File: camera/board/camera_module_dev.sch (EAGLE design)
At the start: 11 parts, among them IC1 74541PW, IC2 74541PW, Q1 MOSFET-NCHANNELBSS123LT1G, Q2 MOSFET-NCHANNELBSS123LT1G

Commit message: Schematic more or less done, moving to layout
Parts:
- added C1: 2.2uF, biomimetic:CAP0402-CAP
- added C10, C11, C12, C7: 1uF, biomimetic:CAP0603-CAP
- added C13, C14, C15, C16, C5, C6, C8, C9: 100nF, biomimetic:CAP0402-CAP
- added C2, C3: 1uF, biomimetic:CAP0402-CAP
- added C4: 10nF, biomimetic:CAP0402-CAP
- added JP3, JP4: (no value), pinhead:PINHD-1X9
- added L1, L2: 3.3uH, biomimetic:INDUCTOR1007
- added R1: 18k, biomimetic:RESISTOR0402-RES
- added R10, R11, R8, R9: 4k7, biomimetic:RESISTOR0402-RES
- added R2: 18k/5k, biomimetic:RESISTOR0402-RES
- added R3, R4, R7: 10k, biomimetic:RESISTOR0402-RES
- added R5: (no value), biomimetic:RESISTOR0402-RES
- added R6: 1k8, biomimetic:RESISTOR0402-RES
- added SJ1, SJ10, SJ11, SJ2, SJ3, SJ4, SJ5, SJ6, SJ7, SJ8, SJ9: SOLDERJUMPERNO, SparkFun-Passives:SOLDERJUMPERNO
- added SJ12, SJ13, SJ14: (no value), SparkFun-Passives:SOLDERJUMPER_2WAYS
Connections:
- new net +3V3: C1.1, C5.2, C6.2, IC1P.VCC, IC2P.VCC, R11.1, R5.1, R9.1, SJ12.3, SJ13.3, U$3G$2.AVDD, U$4.6, U$6G$1.V+
- new net D0: IC1A.A1, SJ1.2, U$1G$1.DATA0, U$2G$1.DATA0, U$3G$1.DATA0
- new net D1: IC1A.A2, SJ2.2, U$1G$1.DATA1, U$2G$1.DATA1, U$3G$1.DATA1
- new net D2: IC1A.A3, SJ3.2, U$1G$1.DATA2, U$2G$1.DATA2, U$3G$1.DATA2
- new net D3: IC1A.A4, SJ4.2, U$1G$1.DATA3, U$2G$1.DATA3, U$3G$1.DATA3
- new net D4: IC1A.A5, SJ5.2, U$1G$1.DATA4, U$2G$1.DATA4, U$3G$1.DATA4
- new net D5: IC1A.A6, SJ6.2, U$1G$1.DATA5, U$2G$1.DATA5, U$3G$1.DATA5
- new net D6: IC1A.A7, SJ7.2, U$1G$1.DATA6, U$2G$1.DATA6, U$3G$1.DATA6
- new net D7: IC1A.A8, SJ8.2, U$1G$1.DATA7, U$2G$1.DATA7, U$3G$1.DATA7
- new net GND: C1.2, C10.2, C11.1, C12.2, C13.2, C14.1, C15.1, C16.2, C2.2, C3.2, C4.1, C5.1, C6.1, C7.1, C8.2, C9.2, IC1P.GND, IC2A.A4, IC2A.A5, IC2A.A6, IC2A.A7, IC2A.A8, IC2P.GND, JP3.9, JP4.9, QG1.VSS, R3.2, R4.2, R7.1, SJ12.1, SJ13.1, U$1G$2.GND, U$2G$2.GND, U$2IOVSS.V, U$3G$2.GND, U$4.11, U$5.11, U$6G$1.GND
- new net HSYNC: IC2A.A3, SJ11.2, U$1G$1.HREF, U$2G$1.HREF, U$3G$1.HREF
- new net N$1: QG1.OUT, SJ14.3
- new net N$10: IC2A.G1, SJ12.2
- new net N$19: R1.2, R4.1, U$6LDOB.FB
- new net N$2: JP3.8, U$4.10
- new net N$21: R2.2, R3.1, U$6LDOA.FB
- new net N$3: R6.1, R7.2, SJ14.1
- new net N$4: C13.1, U$1VREF2.V
- new net N$5: C9.1, U$1VREF1.V
- new net N$6: C12.1, C14.2, C16.1, C7.2, L2.2, U$1G$2.AVDD, U$2G$2.DVDD
- new net N$7: IC1A.G1, SJ13.2
- new net N$8: C10.1, C11.2, C15.2, C8.1, L1.2, U$1G$2.DVDD, U$2G$2.AVDD, U$2IOVDD.V
- new net PCLK: IC2A.A1, SJ9.2, U$1G$1.PCLK, U$2G$1.PCLK, U$3G$1.PCLK
- new net PMOD_D0: IC1A.Y1, JP4.1, SJ1.1, U$5.1
- new net PMOD_D1: IC1A.Y2, JP4.2, SJ2.1, U$5.2
- new net PMOD_D2: IC1A.Y3, JP4.3, SJ3.1, U$5.3
- new net PMOD_D3: IC1A.Y4, JP4.4, SJ4.1, U$5.4
- new net PMOD_D4: IC1A.Y5, JP4.5, SJ5.1, U$5.7
- new net PMOD_D5: IC1A.Y6, JP4.6, SJ6.1, U$5.8
- new net PMOD_D6: IC1A.Y7, IC1A.Y8, JP4.7, SJ7.1, SJ8.1, U$5.9
- new net PMOD_D7: JP4.8, U$5.10
- new net PMOD_HSYNC: IC2A.Y3, JP3.7, SJ11.1, U$4.9
- new net PMOD_PCLK: IC2A.Y1, JP3.5, SJ9.1, U$4.7
- new net PMOD_RESET: IC1A.G2, IC2A.G2, JP3.1, QG1.CON, R5.2, U$1G$1.PWDN, U$2G$1.PWDN, U$3G$1.PWDN, U$4.1, U$6CTRL.EN
- new net PMOD_SCL: JP3.3, Q2.D, R9.2, U$4.3
- new net PMOD_SDA: JP3.4, Q1.D, R11.2, U$4.4
- new net PMOD_VSYNC: IC2A.Y2, JP3.6, SJ10.1, U$4.8
- new net PMOD_XCLK: JP3.2, R6.2, U$4.2
- new net SCL: Q2.S, R8.2, U$1G$1.SCL, U$2G$1.SCL, U$3G$1.SCL
- new net SDA: Q1.S, R10.2, U$1G$1.SDA, U$2G$1.SDA, U$3G$1.SDA
- new net VCCIO: C2.1, C4.2, L1.1, Q1.G, Q2.G, QG1.VDD, R1.1, R10.1, R8.1, U$6LDOB.OUT
- new net VDD: C3.1, L2.1, R2.1, U$6LDOA.OUT
- new net VSYNC: IC2A.A2, SJ10.2, U$1G$1.VSYNC, U$2G$1.VSYNC, U$3G$1.VSYNC
- new net XCLK: SJ14.2, U$1G$1.XVCLK, U$2G$1.XVCLK, U$3G$1.XVCLK
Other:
- moved on the sheet: IC1, IC2, Q1, Q2, QG1, U$1VREF1, U$1VREF2, U$2IOVDD, U$2IOVSS, U$4, U$6CTRL, U$6LDOA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

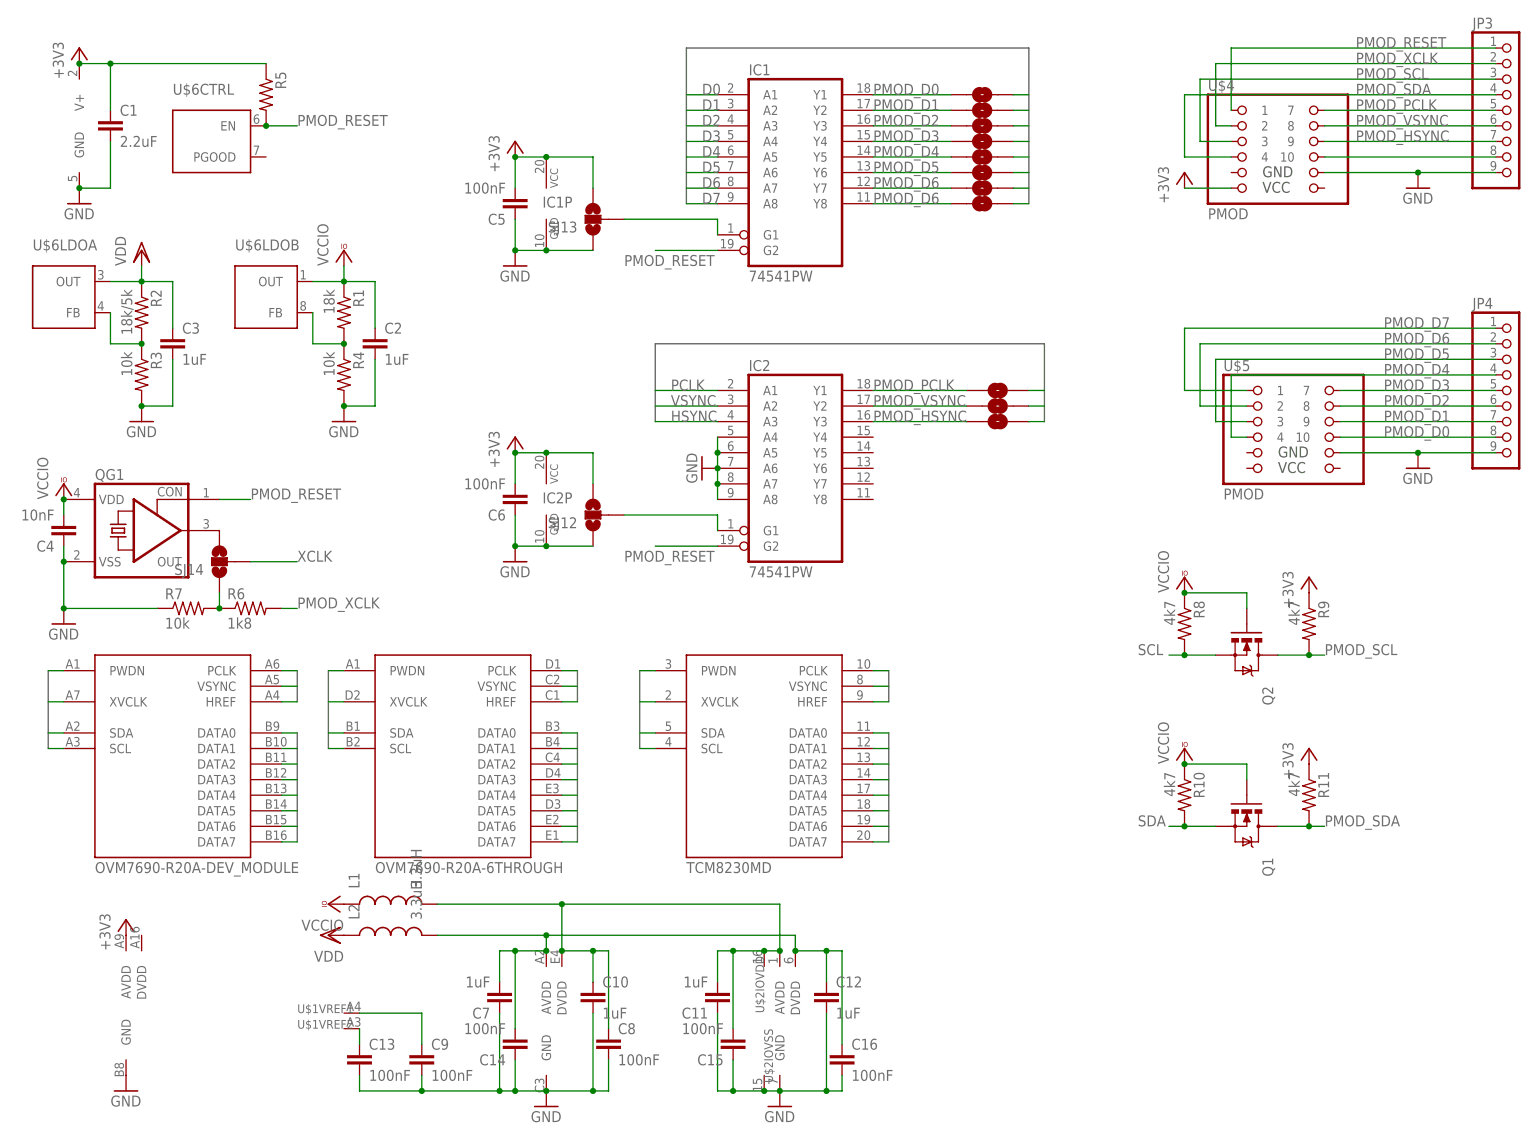
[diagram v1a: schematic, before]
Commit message: Pmod signal routing more or less done
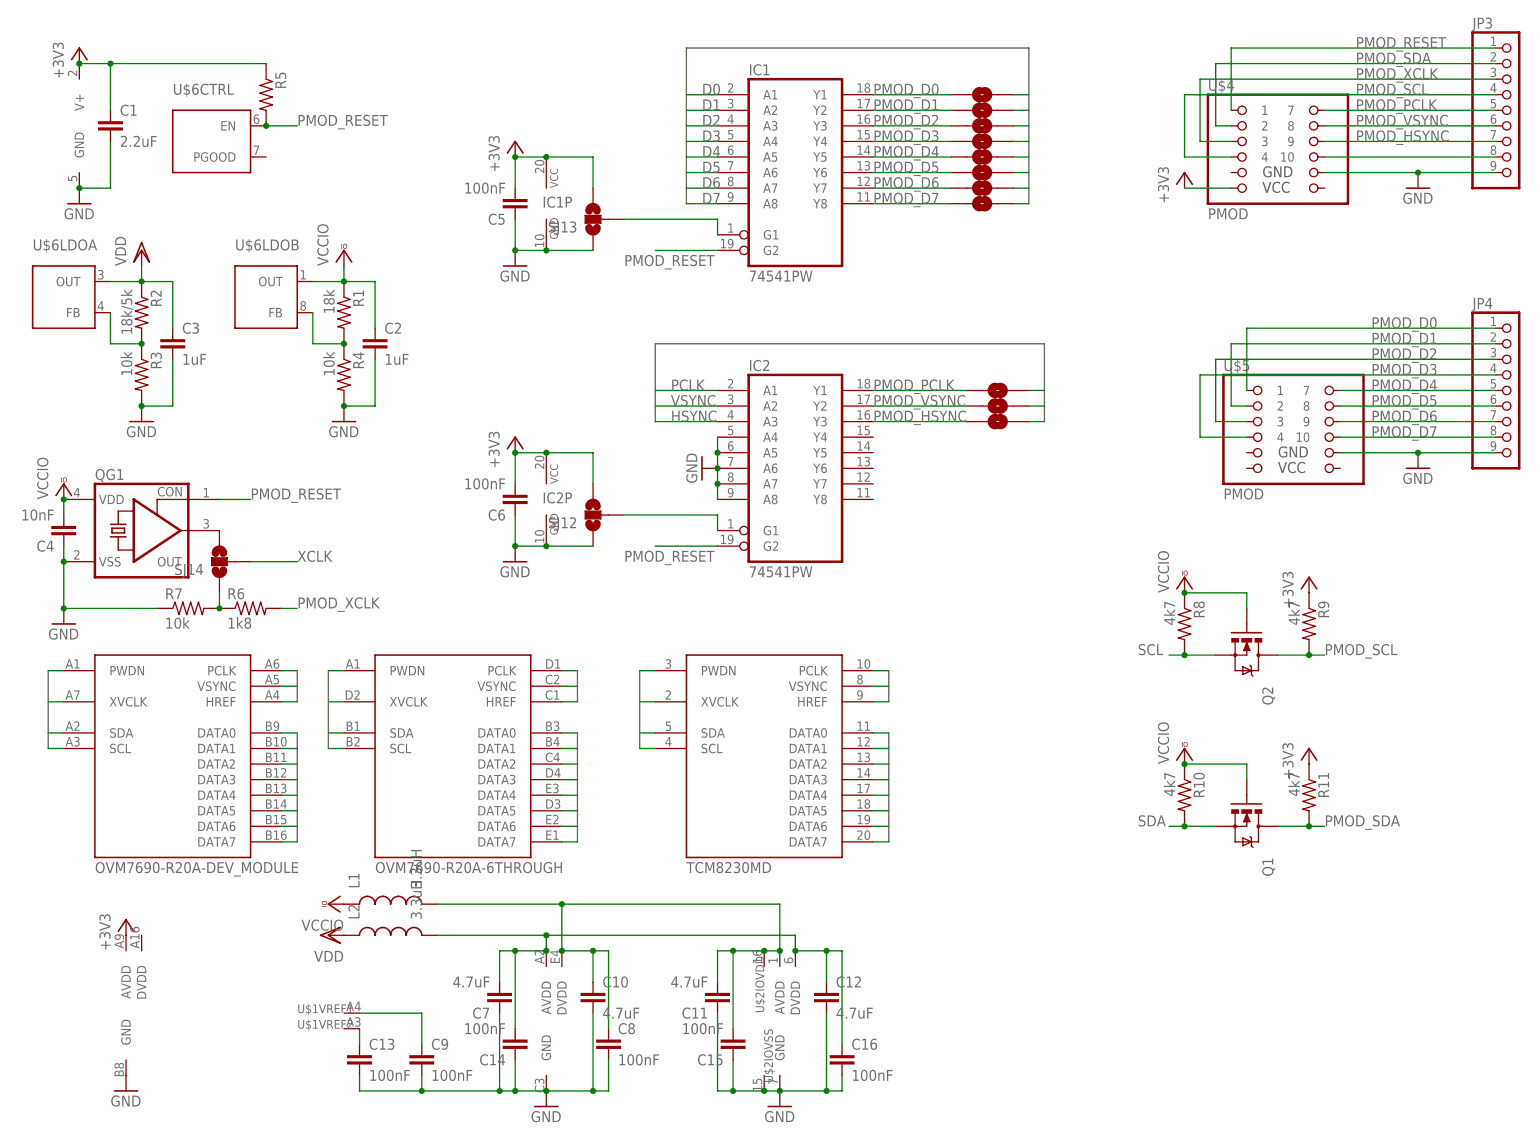
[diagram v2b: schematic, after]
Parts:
- C10, C11, C12, C7: value 1uF -> 4.7uF
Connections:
- net PMOD_D6: no longer IC1A.Y8, SJ8.1
- net PMOD_D7: now also IC1A.Y8, SJ8.1
- net PMOD_SCL: now also JP3.4, U$4.4; no longer JP3.3, U$4.3
- net PMOD_SDA: now also JP3.2, U$4.2; no longer JP3.4, U$4.4
- net PMOD_XCLK: now also JP3.3, U$4.3; no longer JP3.2, U$4.2

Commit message: Most layout done
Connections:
- net +3V3: now also U$3G$2.DVDD; no longer U$3G$2.AVDD
- net N$19: now also U$6LDOA.FB; no longer U$6LDOB.FB
- net N$21: now also U$6LDOB.FB; no longer U$6LDOA.FB
- net VCCIO: now also U$6LDOA.OUT; no longer U$6LDOB.OUT
- net VDD: now also U$6LDOB.OUT; no longer U$6LDOA.OUT
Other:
- moved on the sheet: U$6LDOA, U$6LDOB
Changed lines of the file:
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@@
 <instance part="U$6" gate="G$1" x="10.16" y="165.1"/>
 <instance part="U$6" gate="CTRL" x="38.1" y="157.48"/>
-<instance part="U$6" gate="LDOB" x="45.72" y="132.08"/>
-<instance part="U$6" gate="LDOA" x="12.7" y="132.08"/>
+<instance part="U$6" gate="LDOA" x="45.72" y="132.08"/>
+<instance part="U$6" gate="LDOB" x="12.7" y="132.08"/>
 <instance part="Q1" gate="G$1" x="200.66" y="50.8" smashed="yes" rot="R270">
 <attribute name="NAME" x="203.2" y="45.72" size="1.778" layer="95" rot="R270"/>
@@
 <instance part="VCC4" gate="G$1" x="190.5" y="63.5"/>
 <instance part="GND9" gate="1" x="111.76" y="109.22" rot="R270"/>
-<instance part="+3V7" gate="G$1" x="17.78" y="35.56"/>
+<instance part="+3V7" gate="G$1" x="20.32" y="38.1"/>
 <instance part="GND10" gate="1" x="17.78" y="7.62"/>
 <instance part="GND11" gate="1" x="86.36" y="5.08"/>
@@
 </segment>
 <segment>
-<pinref part="U$3" gate="G$2" pin="AVDD"/>
+<pinref part="U$3" gate="G$2" pin="DVDD"/>
 <pinref part="+3V7" gate="G$1" pin="+3V3"/>
+<wire x1="20.32" y1="33.02" x2="20.32" y2="35.56" width="0.1524" layer="91"/>
 </segment>
 </net>
@@
 <pinref part="R1" gate="G$1" pin="2"/>
 <pinref part="R4" gate="G$1" pin="1"/>
-<pinref part="U$6" gate="LDOB" pin="FB"/>
+<pinref part="U$6" gate="LDOA" pin="FB"/>
 <wire x1="48.26" y1="134.62" x2="48.26" y2="129.54" width="0.1524" layer="91"/>
 <wire x1="48.26" y1="129.54" x2="53.34" y2="129.54" width="0.1524" layer="91"/>
@@
 <pinref part="R2" gate="G$1" pin="2"/>
 <pinref part="R3" gate="G$1" pin="1"/>
-<pinref part="U$6" gate="LDOA" pin="FB"/>
+<pinref part="U$6" gate="LDOB" pin="FB"/>
 <wire x1="20.32" y1="129.54" x2="15.24" y2="129.54" width="0.1524" layer="91"/>
 <wire x1="15.24" y1="129.54" x2="15.24" y2="134.62" width="0.1524" layer="91"/>
@@
 <net name="VDD" class="0">
 <segment>
-<pinref part="U$6" gate="LDOA" pin="OUT"/>
+<pinref part="U$6" gate="LDOB" pin="OUT"/>
 <pinref part="R2" gate="G$1" pin="1"/>
 <wire x1="15.24" y1="139.7" x2="20.32" y2="139.7" width="0.1524" layer="91"/>
@@
 <net name="VCCIO" class="0">
 <segment>
-<pinref part="U$6" gate="LDOB" pin="OUT"/>
+<pinref part="U$6" gate="LDOA" pin="OUT"/>
 <pinref part="R1" gate="G$1" pin="1"/>
 <wire x1="48.26" y1="139.7" x2="53.34" y2="139.7" width="0.1524" layer="91"/>
@@
 </segment>
 <segment>
+<pinref part="U$3" gate="G$1" pin="DATA5"/>
+<wire x1="43.18" y1="53.34" x2="45.72" y2="53.34" width="0.1524" layer="91"/>
+</segment>
+<segment>
 <pinref part="U$1" gate="G$1" pin="DATA5"/>
 <wire x1="88.9" y1="53.34" x2="91.44" y2="53.34" width="0.1524" layer="91"/>
 </segment>
-<segment>
-<pinref part="U$3" gate="G$1" pin="DATA5"/>
-<wire x1="43.18" y1="53.34" x2="45.72" y2="53.34" width="0.1524" layer="91"/>
-</segment>
-</net>
+</net>

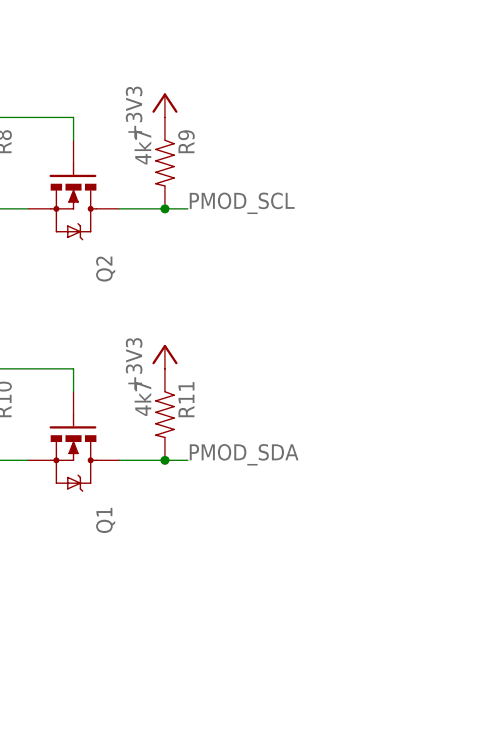
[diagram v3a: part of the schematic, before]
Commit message: Fixing small things preparing for panelization
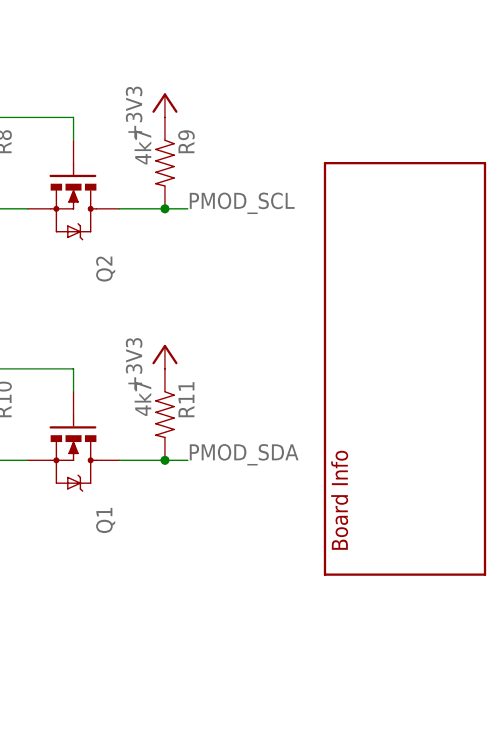
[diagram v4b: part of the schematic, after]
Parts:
- added U$7: INFO, modular_robotics:INFO
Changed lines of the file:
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@@
 <attribute name="VOLTAGE" value="6.3V"/>
+</part>
+<part name="U$7" library="modular_robotics" deviceset="INFO" device="">
+<attribute name="AUTHOR" value="Austin Buchan"/>
+<attribute name="DATE" value="Feb. 2014"/>
+<attribute name="DESIGN" value="Dev Camera Module"/>
+<attribute name="ORGANIZATION" value="UC Berkeley Biomimetic Millisystems Lab"/>
+<attribute name="REVISION" value="r0.0"/>
 </part>
 </parts>
@@
 <attribute name="VOLTAGE" x="134.62" y="12.7" size="1.778" layer="96" display="off"/>
 </instance>
+<instance part="U$7" gate="G$1" x="243.84" y="40.64" rot="R90">
+<attribute name="DATE" x="243.84" y="40.64" size="1.778" layer="96" rot="R90" display="off"/>
+<attribute name="DESIGN" x="243.84" y="40.64" size="1.778" layer="96" rot="R90" display="off"/>
+<attribute name="ORGANIZATION" x="243.84" y="40.64" size="1.778" layer="96" rot="R90" display="off"/>
+<attribute name="AUTHOR" x="243.84" y="40.64" size="1.778" layer="96" rot="R90" display="off"/>
+<attribute name="REVISION" x="243.84" y="40.64" size="1.778" layer="96" rot="R90" display="off"/>
+</instance>
 </instances>

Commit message: Board and component orders placed
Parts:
- C10, C11, C12, C7: value 4.7uF -> 10uF
- C3: VOLTAGE (none) -> 6.3V
- R2: value 18k/5k -> 18k/5k1
- R5: value (none) -> 10k
- R6: value 1k8 -> 2k
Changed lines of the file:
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@@
 <attribute name="VOLTAGE" value="6.3V"/>
 </part>
-<part name="R2" library="biomimetic" deviceset="RESISTOR" device="0402-RES" value="18k/5k"/>
+<part name="R2" library="biomimetic" deviceset="RESISTOR" device="0402-RES" value="18k/5k1"/>
 <part name="R3" library="biomimetic" deviceset="RESISTOR" device="0402-RES" value="10k"/>
 <part name="GND1" library="supply1" deviceset="GND" device=""/>
@@
 <part name="VCC1" library="supply1" deviceset="VCCIO" device=""/>
 <part name="VDD1" library="supply1" deviceset="VDD" device=""/>
-<part name="C3" library="biomimetic" deviceset="CAP" device="0402-CAP" value="1uF"/>
+<part name="C3" library="biomimetic" deviceset="CAP" device="0402-CAP" value="1uF">
+<attribute name="VOLTAGE" value="6.3V"/>
+</part>
 <part name="R1" library="biomimetic" deviceset="RESISTOR" device="0402-RES" value="18k"/>
 <part name="R4" library="biomimetic" deviceset="RESISTOR" device="0402-RES" value="10k"/>
 <part name="GND2" library="supply1" deviceset="GND" device=""/>
 <part name="GND3" library="supply1" deviceset="GND" device=""/>
-<part name="R5" library="biomimetic" deviceset="RESISTOR" device="0402-RES"/>
+<part name="R5" library="biomimetic" deviceset="RESISTOR" device="0402-RES" value="10k"/>
 <part name="GND4" library="supply1" deviceset="GND" device=""/>
 <part name="GND5" library="supply1" deviceset="GND" device=""/>
@@
 <attribute name="VOLTAGE" value="6.3V"/>
 </part>
-<part name="R6" library="biomimetic" deviceset="RESISTOR" device="0402-RES" value="1k8"/>
+<part name="R6" library="biomimetic" deviceset="RESISTOR" device="0402-RES" value="2k"/>
 <part name="R7" library="biomimetic" deviceset="RESISTOR" device="0402-RES" value="10k"/>
 <part name="C6" library="biomimetic" deviceset="CAP" device="0402-CAP" value="100nF">
@@
 <part name="GND11" library="supply1" deviceset="GND" device=""/>
 <part name="GND12" library="supply1" deviceset="GND" device=""/>
-<part name="C7" library="biomimetic" deviceset="CAP" device="0603-CAP" value="4.7uF">
+<part name="C7" library="biomimetic" deviceset="CAP" device="0603-CAP" value="10uF">
 <attribute name="VOLTAGE" value="6.3V"/>
 </part>
@@
 <attribute name="VOLTAGE" value="6.3V"/>
 </part>
-<part name="C10" library="biomimetic" deviceset="CAP" device="0603-CAP" value="4.7uF">
+<part name="C10" library="biomimetic" deviceset="CAP" device="0603-CAP" value="10uF">
 <attribute name="VOLTAGE" value="6.3V"/>
 </part>
 <part name="VCC5" library="supply1" deviceset="VCCIO" device=""/>
 <part name="VDD2" library="supply1" deviceset="VDD" device=""/>
-<part name="C11" library="biomimetic" deviceset="CAP" device="0603-CAP" value="4.7uF">
+<part name="C11" library="biomimetic" deviceset="CAP" device="0603-CAP" value="10uF">
 <attribute name="VOLTAGE" value="6.3V"/>
 </part>
-<part name="C12" library="biomimetic" deviceset="CAP" device="0603-CAP" value="4.7uF">
+<part name="C12" library="biomimetic" deviceset="CAP" device="0603-CAP" value="10uF">
 <attribute name="VOLTAGE" value="6.3V"/>
 </part>
@@
 <instance part="VCC1" gate="G$1" x="53.34" y="144.78"/>
 <instance part="VDD1" gate="G$1" x="20.32" y="144.78"/>
-<instance part="C3" gate="G$1" x="25.4" y="129.54"/>
+<instance part="C3" gate="G$1" x="25.4" y="129.54">
+<attribute name="VOLTAGE" x="25.4" y="129.54" size="1.778" layer="96" display="off"/>
+</instance>
 <instance part="R1" gate="G$1" x="53.34" y="134.62" rot="R270"/>
 <instance part="R4" gate="G$1" x="53.34" y="124.46" rot="R270"/>
